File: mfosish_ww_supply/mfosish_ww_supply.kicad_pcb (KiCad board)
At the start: 2 copper layers, 100 x 61 mm, 31 parts, among them J1 Conn_01x02, J2 Conn_01x03, J3 Conn_01x02, U1 LM7812_TO220, U2 LM7912_TO220

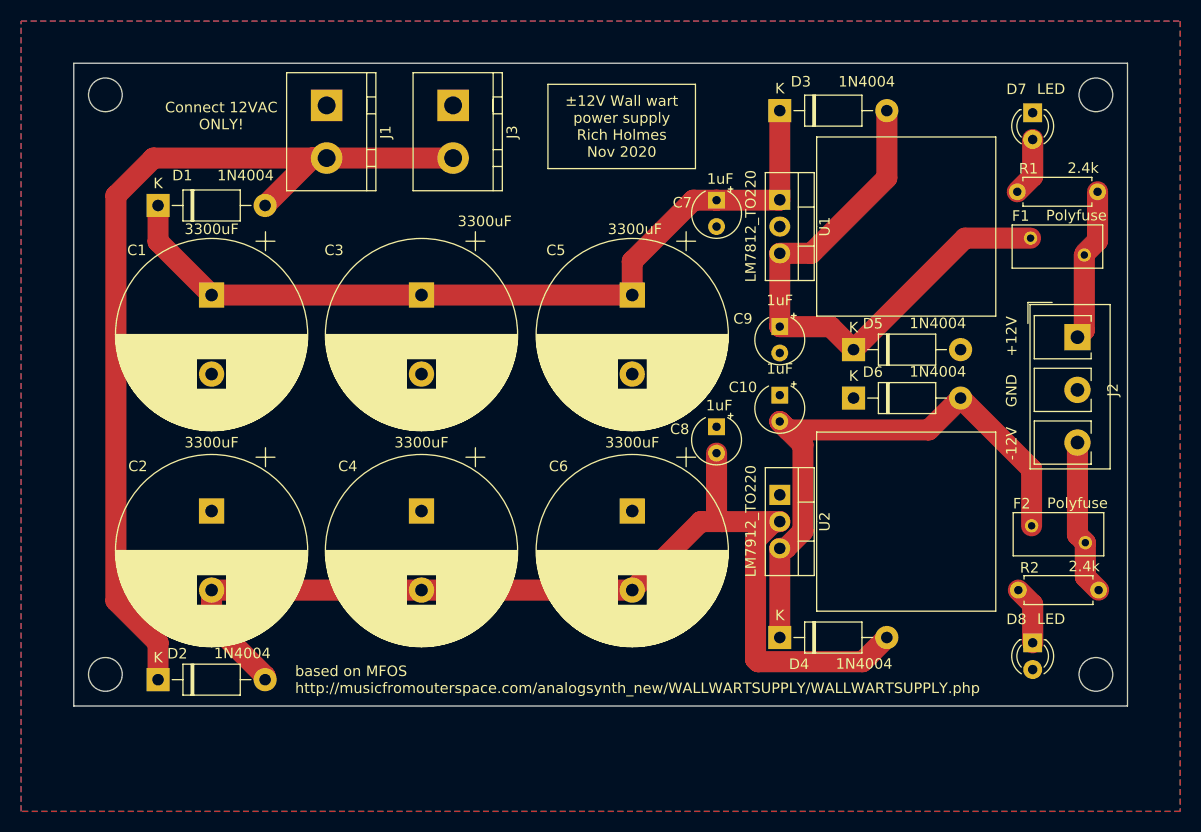
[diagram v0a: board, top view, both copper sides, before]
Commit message: Few tweaks, added barrel jack
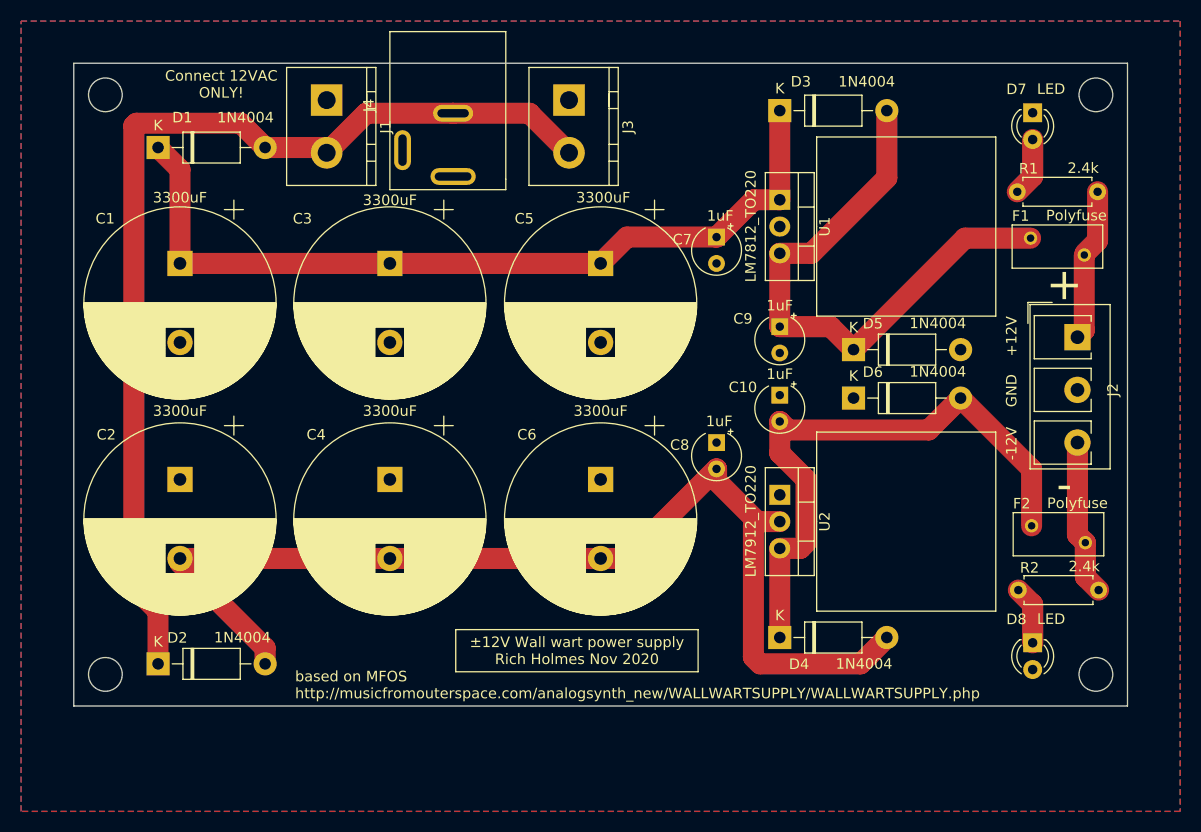
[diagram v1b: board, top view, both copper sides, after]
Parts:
- added J4: Conn_01x02, ao_tht:Wall_wart_A-4118, F.Cu at (86.0, 68.0)
- moved J3 11.0 mm to (97.0, 67.5)
- moved D1 5.50 mm to (58.0, 72.0)
- moved C1 4.24 mm to (60.1, 83.0)
- moved C2 4.24 mm to (60.1, 103.5)
- moved C3 4.24 mm to (80.0, 83.0)
- moved C4 4.24 mm to (80.0, 103.5)
- moved C5 4.24 mm to (100.0, 83.0)
- moved C6 4.24 mm to (100.0, 103.5)
- moved C7 3.50 mm to (111.0, 80.5)
- moved C8 1.50 mm to (111.0, 100.0)
- moved D2 1.50 mm to (58.0, 121.0)
- moved J1 0.50 mm to (74.0, 67.5)
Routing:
- net Net-(D1-Pad2): track 88.8 -> 97.7 mm
- net Net-(C2-Pad2): track 101.9 -> 103.5 mm
- net Net-(C1-Pad1): track 78.7 -> 79.8 mm
- net Net-(C10-Pad2): track 56.3 -> 57.4 mm
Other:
- board text added: "+"
- board text added: "-"

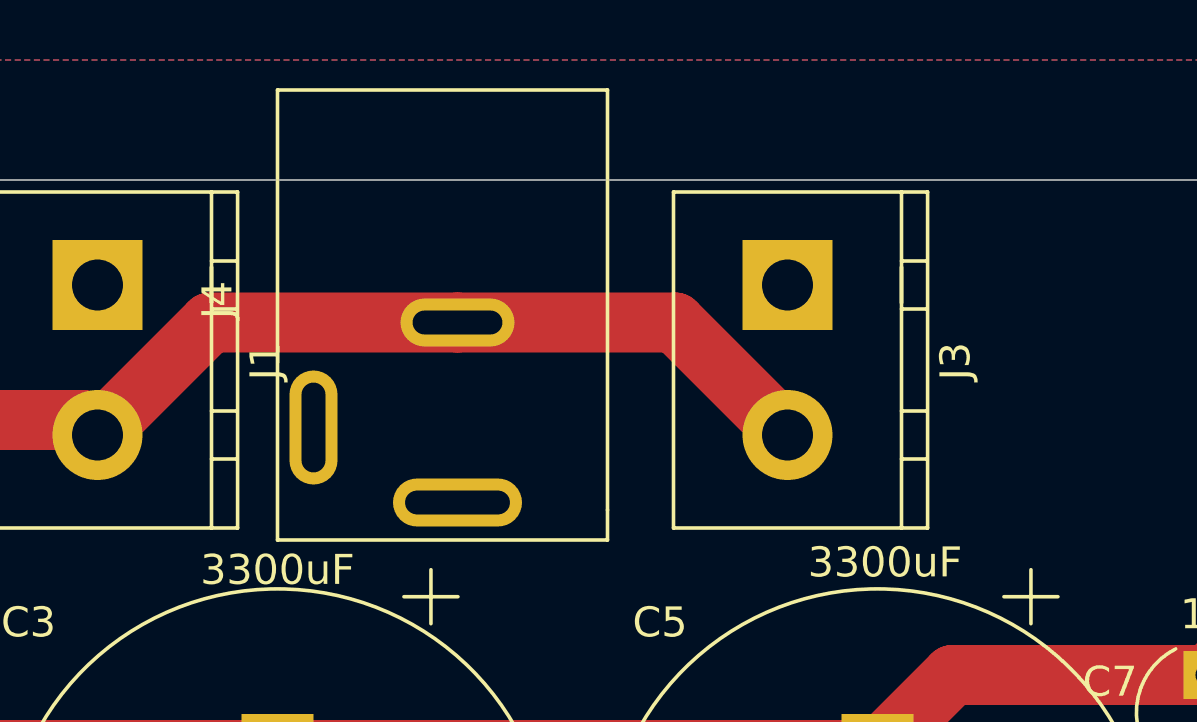
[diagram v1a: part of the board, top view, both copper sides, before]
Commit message: More tweaks, revised jack footprint
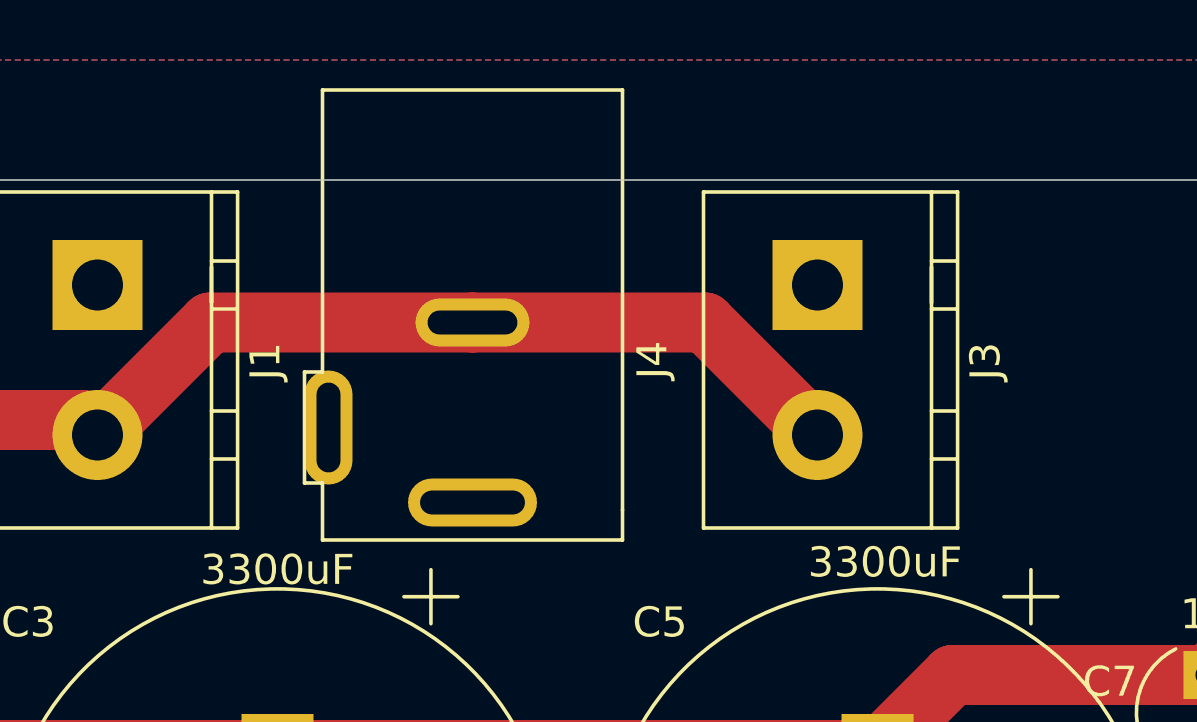
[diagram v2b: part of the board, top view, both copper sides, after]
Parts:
- moved J3 1.00 mm to (98.0, 67.5)
- moved J4 0.50 mm to (86.5, 68.0)
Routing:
- net Net-(D1-Pad2): track 97.7 -> 98.7 mm

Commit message: PCB revisions
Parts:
- added G***: LOGO, ao_tht:analogoutput_12mm, F.Cu at (109.0, 70.5)

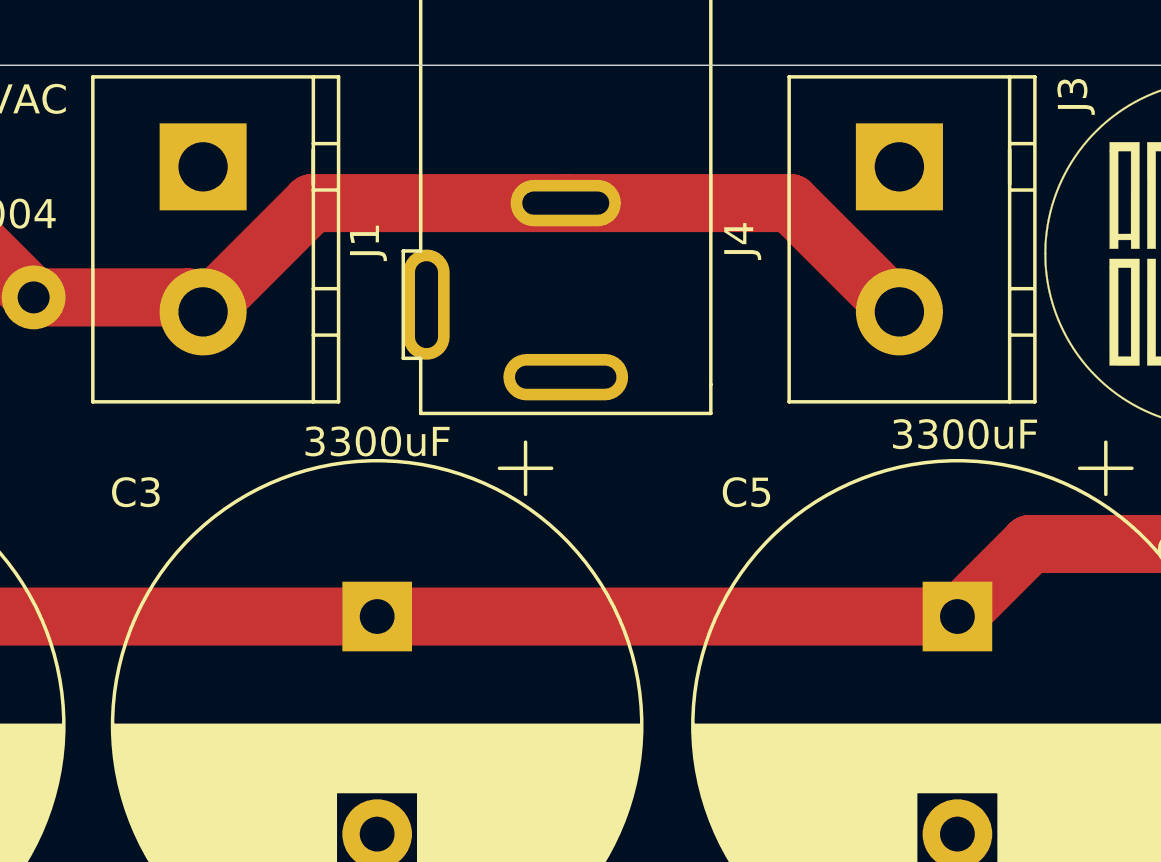
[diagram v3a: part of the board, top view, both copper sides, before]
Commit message: Fix (I hope) misconnected barrel jack
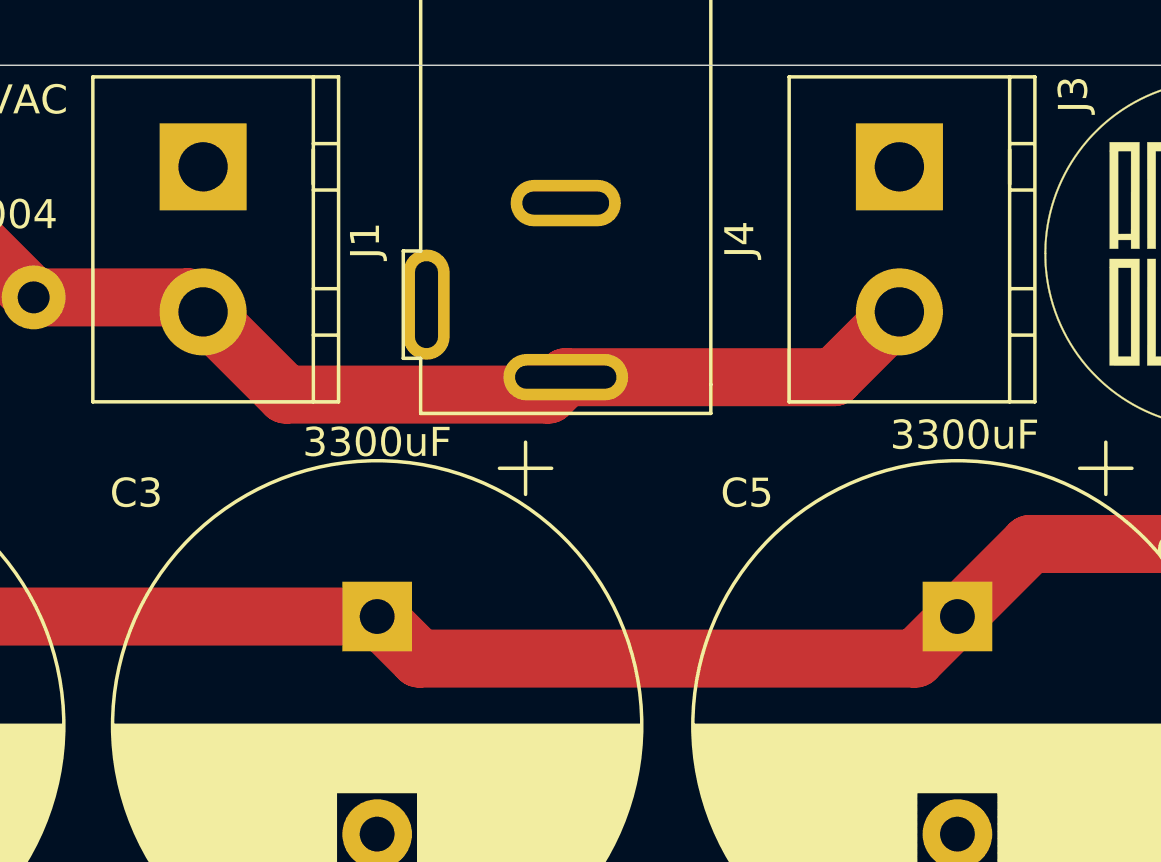
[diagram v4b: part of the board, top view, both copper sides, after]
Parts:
- J4: value Conn_01x02 -> Conn_01x03
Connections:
- J4 pad 1: GND -> Net-(J4-Pad1)
- J4 pad 2: Net-(D1-Pad2) -> GND
- J4 pad 3: (no net) -> Net-(D1-Pad2)
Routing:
- net Net-(C1-Pad1): track 79.8 -> 81.0 mm
- net Net-(D1-Pad2): track 98.7 -> 97.9 mm

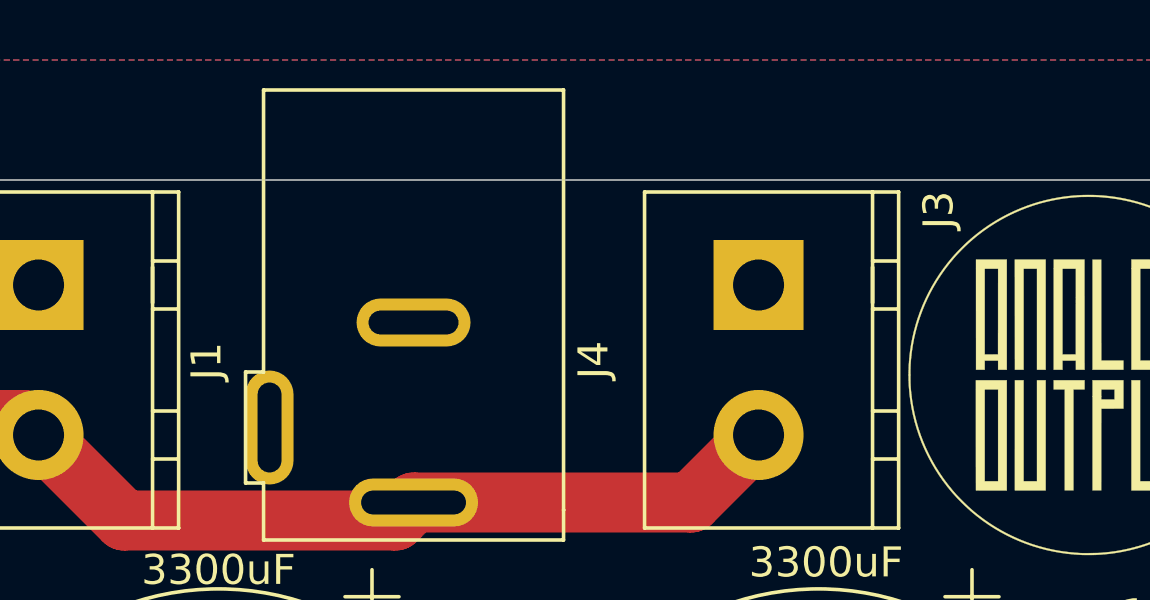
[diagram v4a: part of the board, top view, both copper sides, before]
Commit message: Ground barrel jack switch
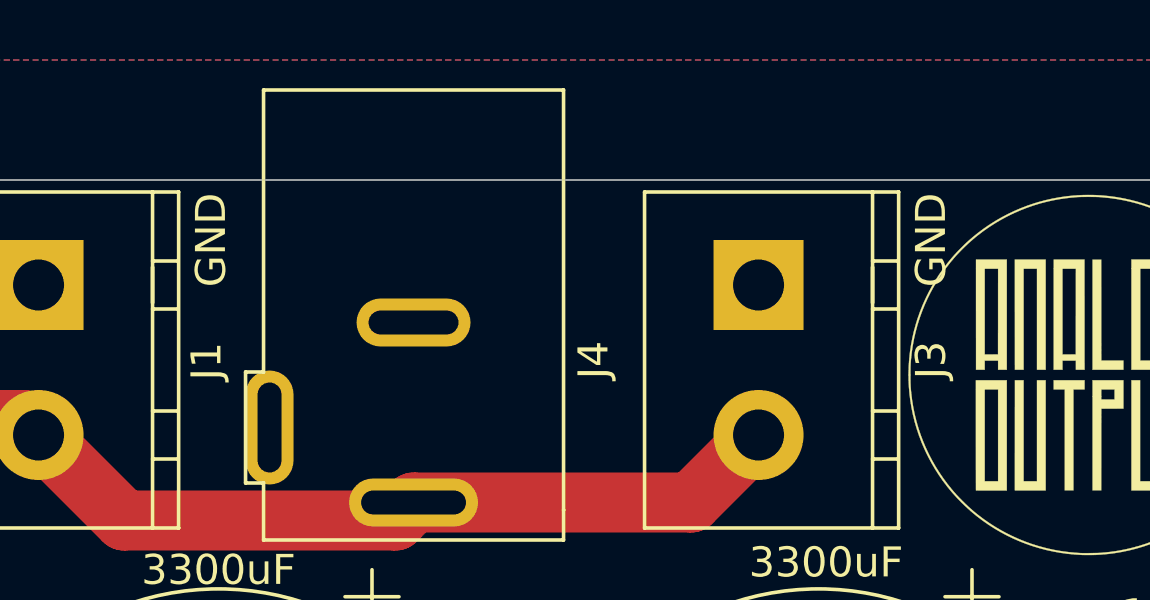
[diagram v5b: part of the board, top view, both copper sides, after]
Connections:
- J4 pad 1: Net-(J4-Pad1) -> GND

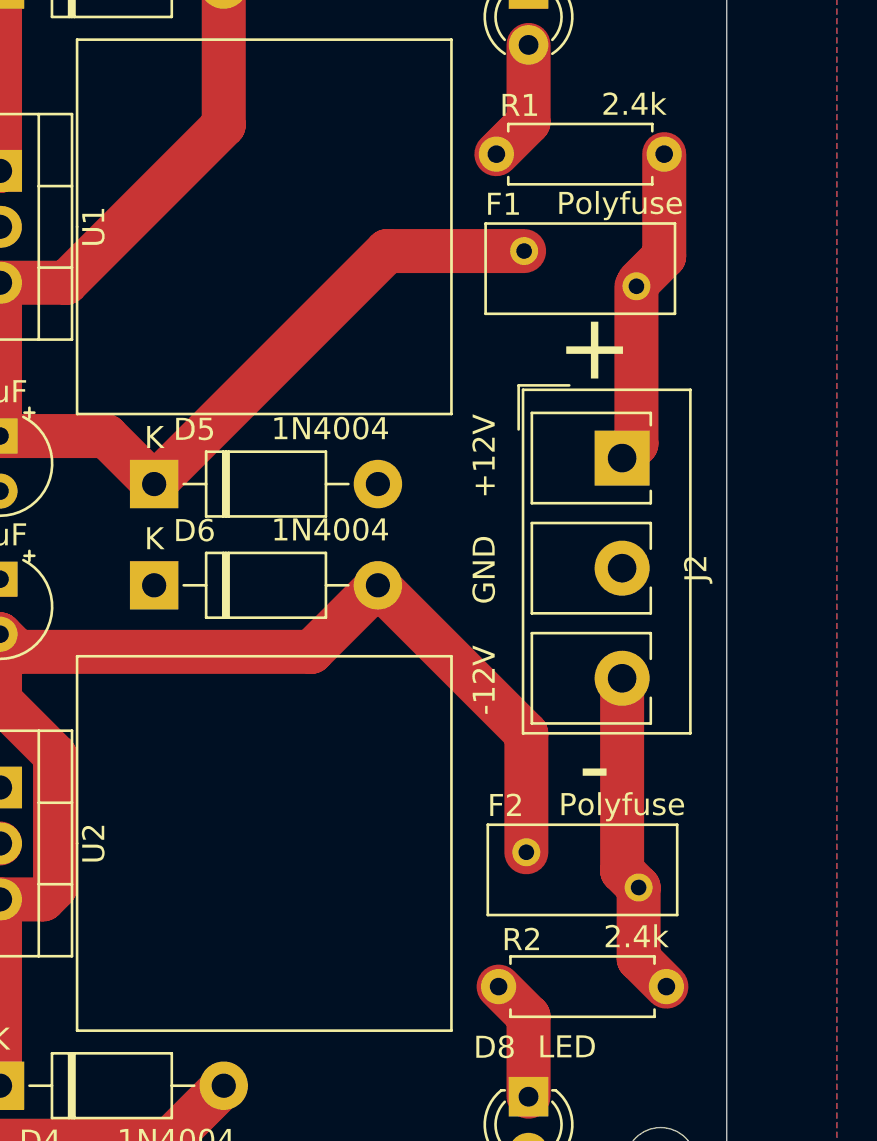
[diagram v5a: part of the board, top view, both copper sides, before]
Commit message: Correct polyswitch footprint
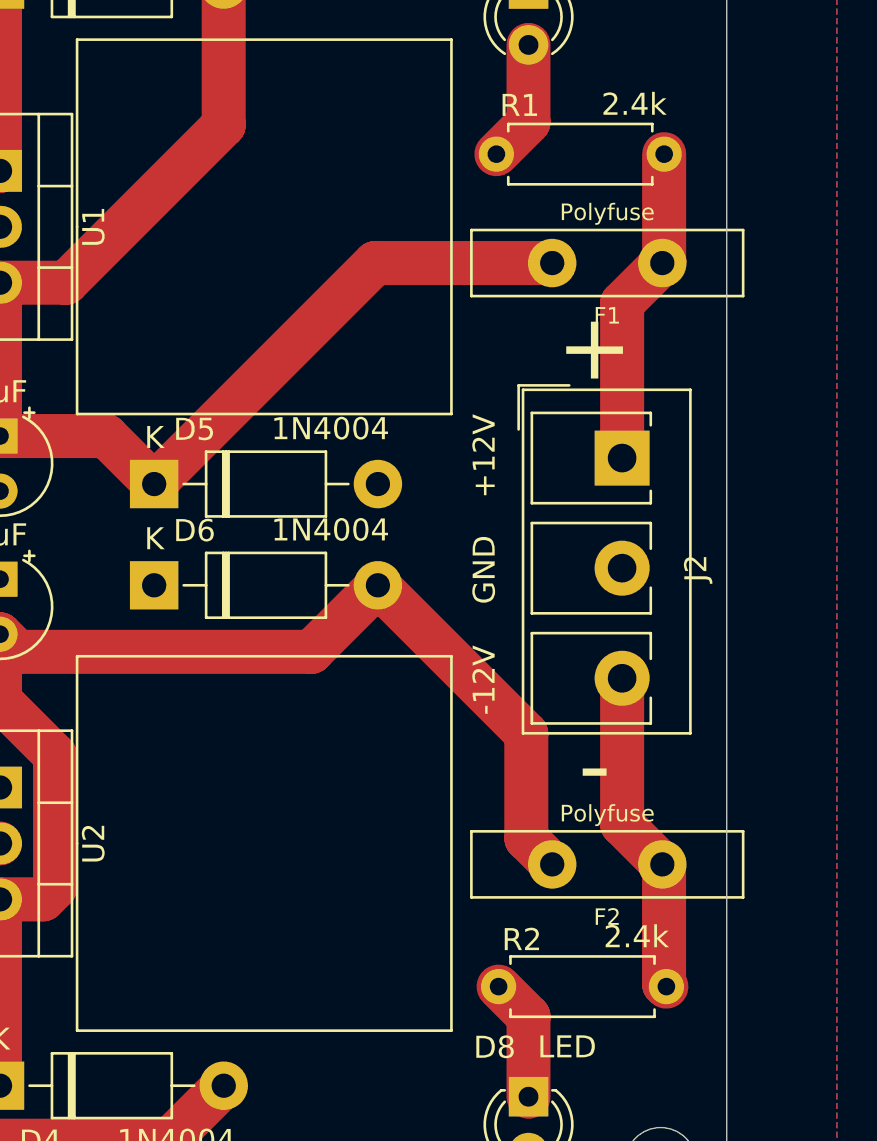
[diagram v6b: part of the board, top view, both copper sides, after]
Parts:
- F1, F2: footprint Fuse:Fuse_BelFuse_0ZRE0005FF_L8.3mm_W3.8mm -> ao_tht:PPTC_RXEF110
- moved F2 1.77 mm to (144.6, 108.5)
- moved F1 1.69 mm to (144.6, 81.1)
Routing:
- net Net-(C9-Pad1): track 55.6 -> 56.6 mm
- net Net-(C10-Pad2): track 57.4 -> 58.4 mm
